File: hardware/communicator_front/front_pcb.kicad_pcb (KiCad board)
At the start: 2 copper layers, 148 x 81 mm, 15 parts, among them U1 ICM7555xB

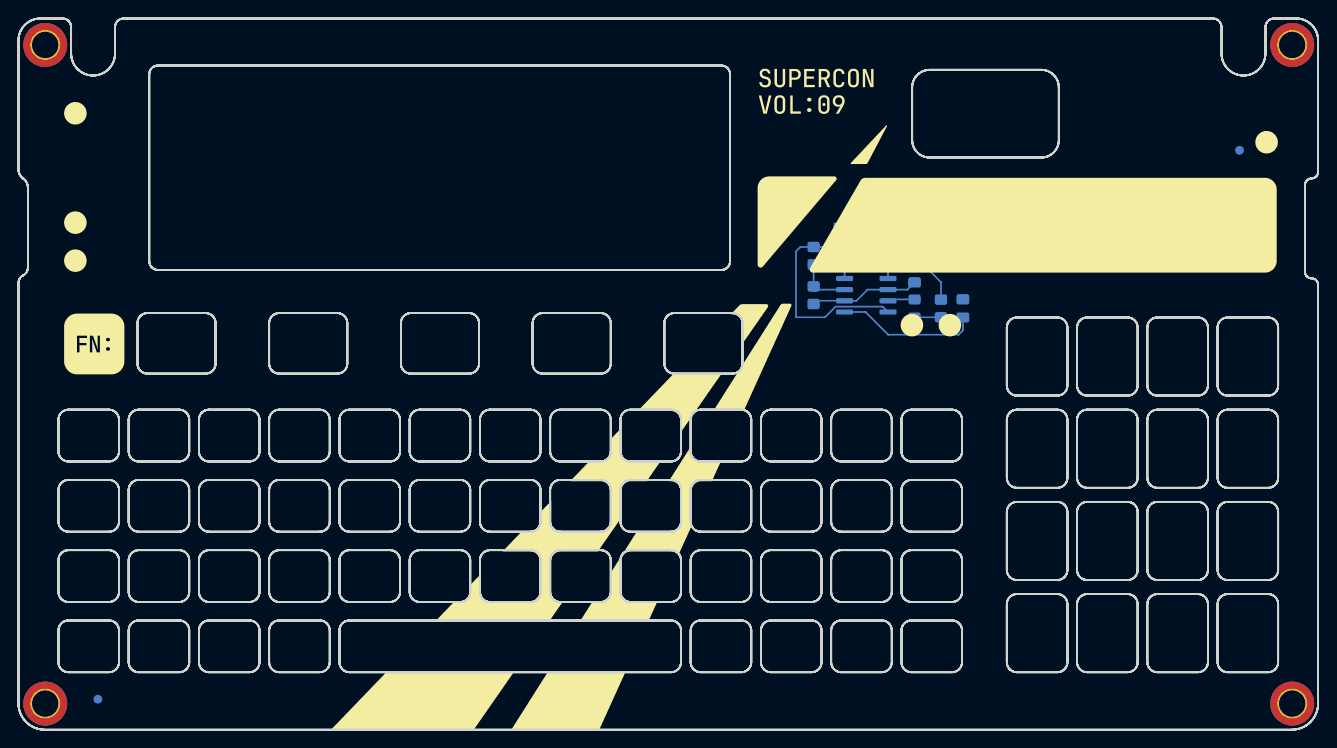
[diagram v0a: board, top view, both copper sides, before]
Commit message: fixed outline issues on front pcb
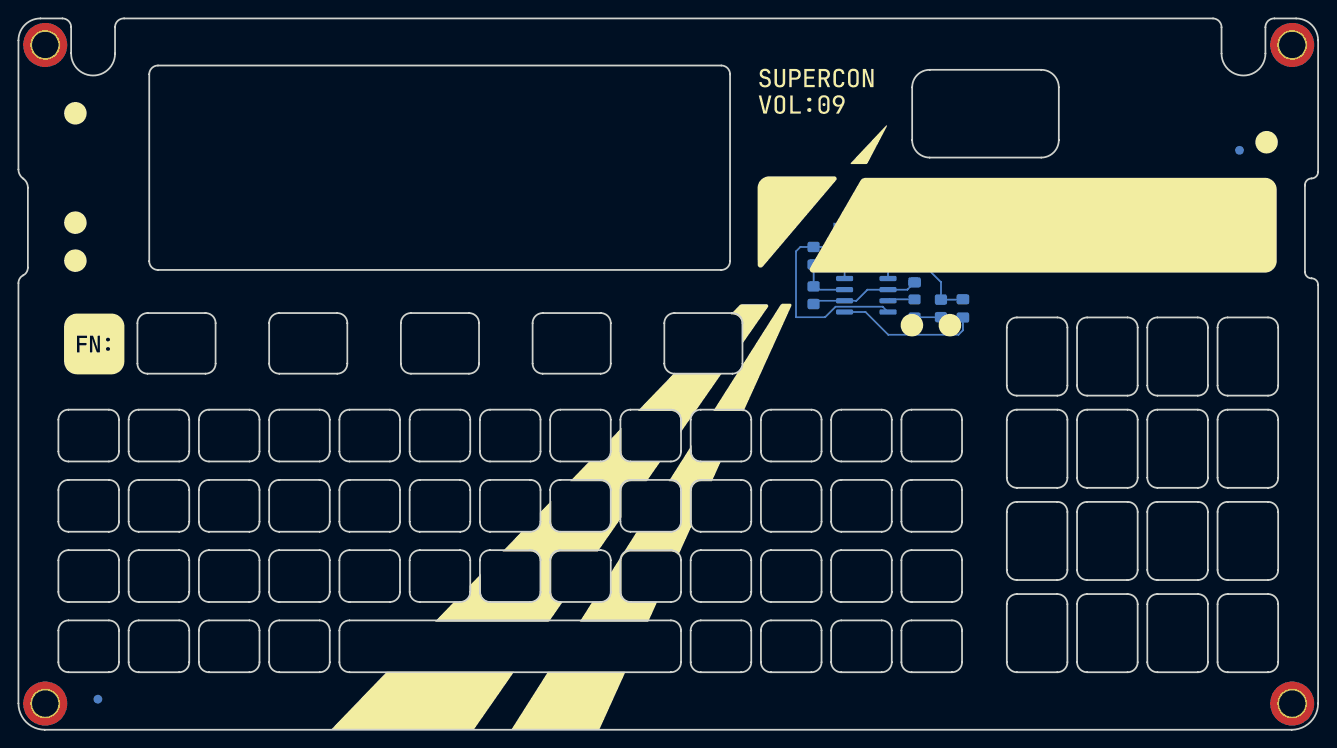
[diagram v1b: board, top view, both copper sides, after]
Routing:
- net GND: track 15.7 -> 18.2 mm
